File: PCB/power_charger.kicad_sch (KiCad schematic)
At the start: 10 parts

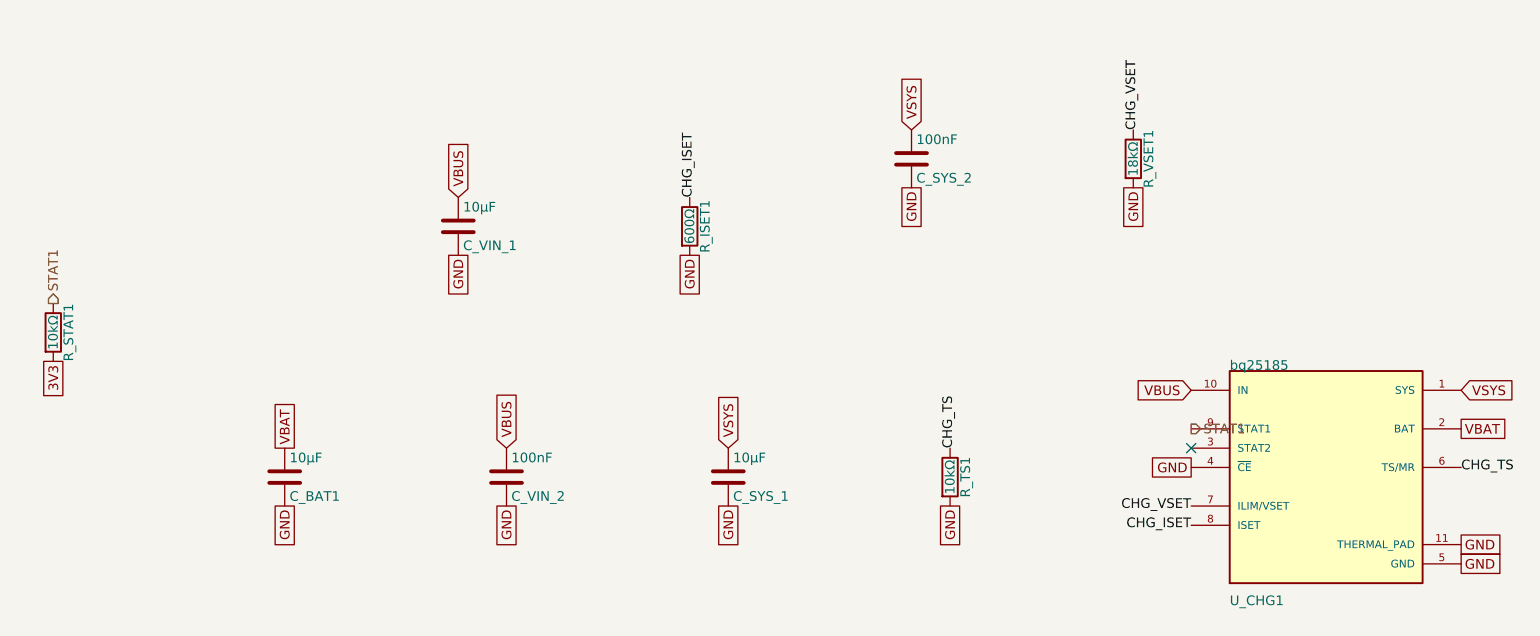
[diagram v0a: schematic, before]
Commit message: Fix footprints and begin layout (#17)
* refactor: updated gulikit footprint

This updates the gulikit thumbstick footprint to be accurate.

* layout: beginning pcb layout

This updates the schematic with a few different footprints while also starts the layout.
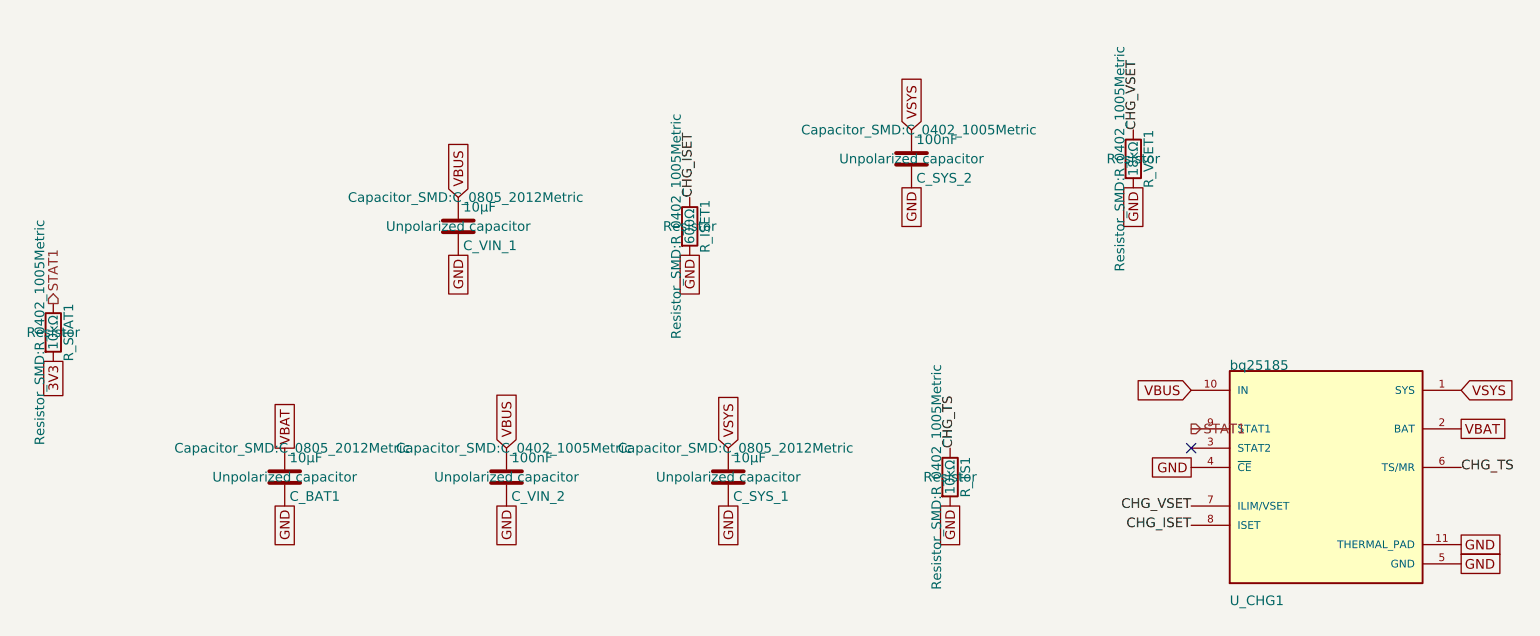
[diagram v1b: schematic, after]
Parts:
- U_CHG1: Description_1 1-cell, 1-A stand-alone linear battery charger with power p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 -> (none)

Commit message: refactor: swap footprints and add symmetry
This updates the footprints of a couple components to be smaller and closer to what we want. It also adds two buttons to ensure left and right side symmetry.
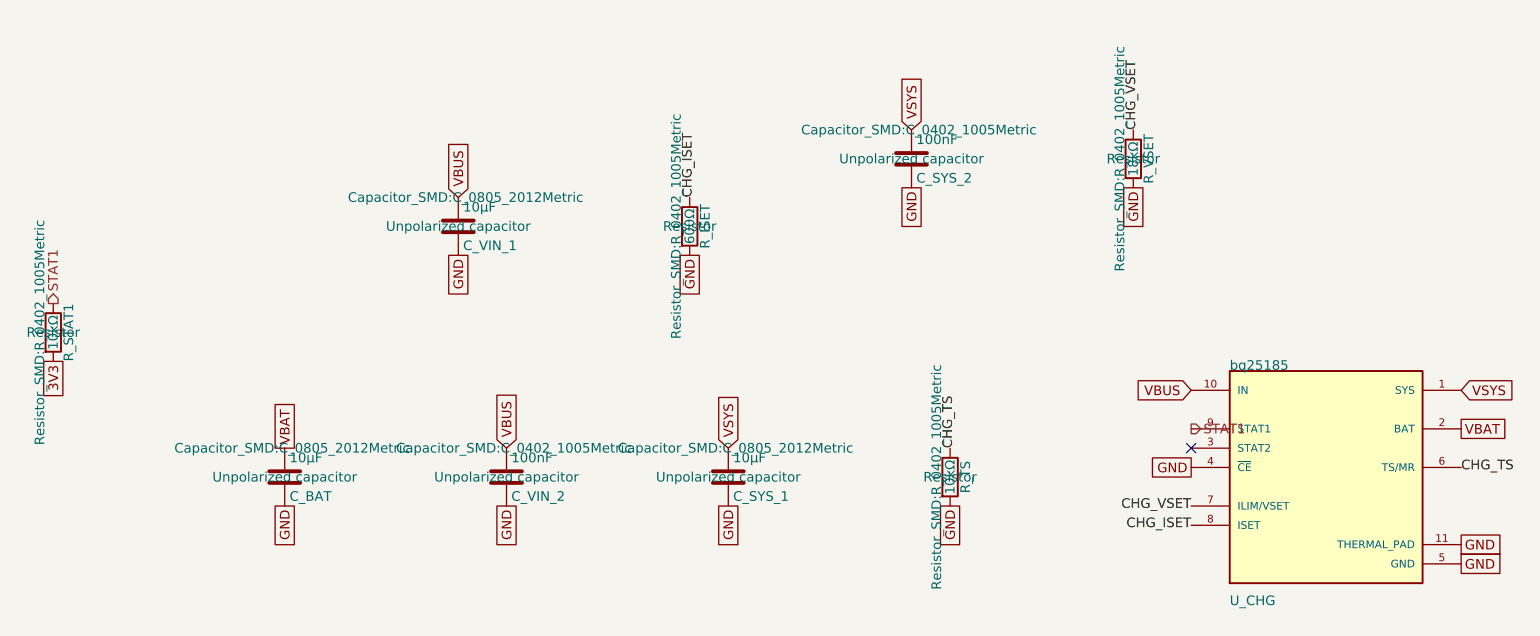
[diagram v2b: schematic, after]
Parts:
- removed C_BAT1: 10µF, Capacitor_SMD:C_0805_2012Metric, symbol Device:C
- removed R_ISET1: 600Ω, Resistor_SMD:R_0402_1005Metric, symbol Device:R
- removed R_TS1: 10kΩ, Resistor_SMD:R_0402_1005Metric, symbol Device:R
- removed R_VSET1: 18kΩ, Resistor_SMD:R_0402_1005Metric, symbol Device:R
- removed U_CHG1: bq25185, BQ25185DLHR:IC_BQ25185DLHR, symbol BQ25185DLHR:BQ25185DLHR
- added C_BAT: 10µF, Capacitor_SMD:C_0805_2012Metric, symbol Device:C
- added R_ISET: 600Ω, Resistor_SMD:R_0402_1005Metric, symbol Device:R
- added R_TS: 10kΩ, Resistor_SMD:R_0402_1005Metric, symbol Device:R
- added R_VSET: 18kΩ, Resistor_SMD:R_0402_1005Metric, symbol Device:R
- added U_CHG: bq25185, BQ25185DLHR:IC_BQ25185DLHR, symbol BQ25185DLHR:BQ25185DLHR
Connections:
- net CHG_ISET: now also R_ISET.1, U_CHG.8 (ISET)
- net CHG_TS: now also R_TS.1, U_CHG.6 (TS/MR)
- net CHG_VSET: now also R_VSET.1, U_CHG.7 (ILIM/VSET)
- net GND: now also C_BAT.2, R_ISET.2, R_TS.2, R_VSET.2, U_CHG.11 (THERMAL_PAD), U_CHG.4 (~{CE}), U_CHG.5 (GND)
- net STAT1: now also U_CHG.9 (STAT1)
- net VBAT: now also C_BAT.1, U_CHG.2 (BAT)
- net VBUS: now also U_CHG.10 (IN)
- net VSYS: now also U_CHG.1 (SYS)

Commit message: layout: everything is on the board
The board edge cuts are down to 100mm x 35mm. All the components have the right footprints and are on the board, but no traces exist yet, and not all circuits are laid out properly yet. Lots of DRC warnings.
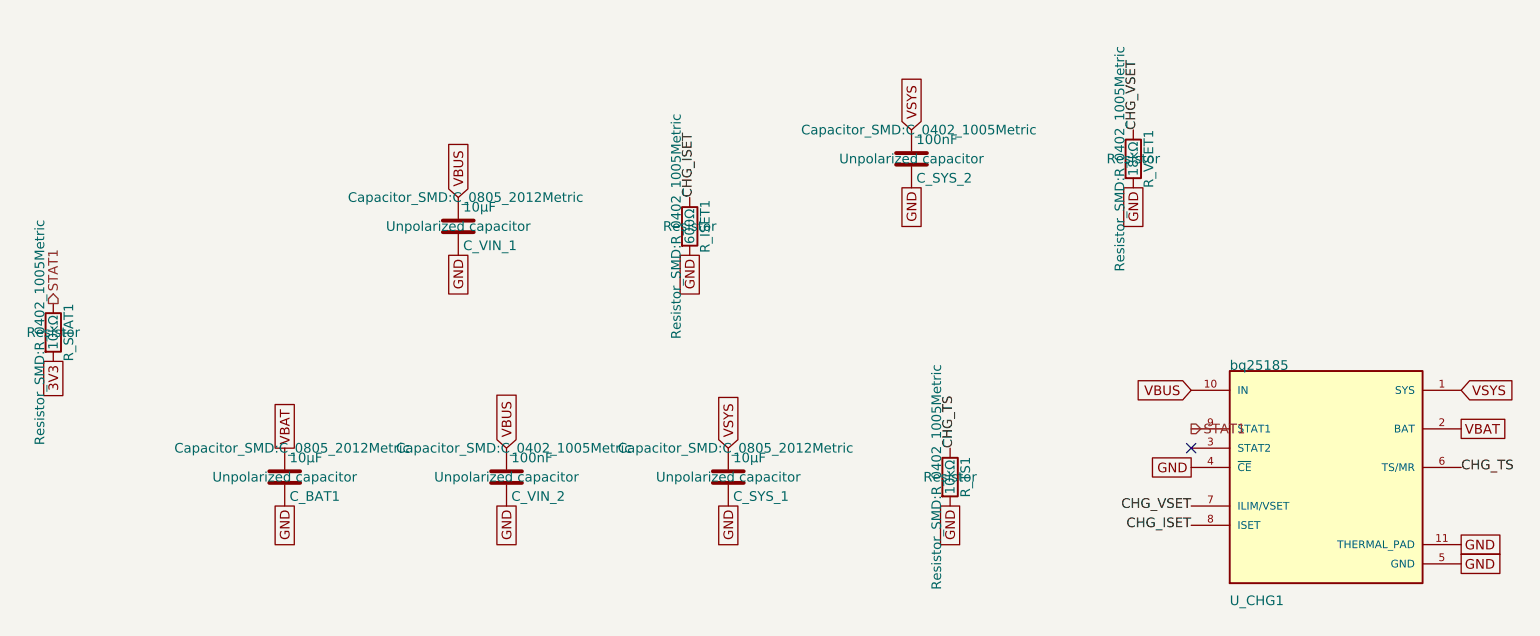
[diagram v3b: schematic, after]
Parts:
- removed C_BAT: 10µF, Capacitor_SMD:C_0805_2012Metric, symbol Device:C
- removed R_ISET: 600Ω, Resistor_SMD:R_0402_1005Metric, symbol Device:R
- removed R_TS: 10kΩ, Resistor_SMD:R_0402_1005Metric, symbol Device:R
- removed R_VSET: 18kΩ, Resistor_SMD:R_0402_1005Metric, symbol Device:R
- removed U_CHG: bq25185, BQ25185DLHR:IC_BQ25185DLHR, symbol BQ25185DLHR:BQ25185DLHR
- added C_BAT1: 10µF, Capacitor_SMD:C_0805_2012Metric, symbol Device:C
- added R_ISET1: 600Ω, Resistor_SMD:R_0402_1005Metric, symbol Device:R
- added R_TS1: 10kΩ, Resistor_SMD:R_0402_1005Metric, symbol Device:R
- added R_VSET1: 18kΩ, Resistor_SMD:R_0402_1005Metric, symbol Device:R
- added U_CHG1: bq25185, BQ25185DLHR:IC_BQ25185DLHR, symbol BQ25185DLHR:BQ25185DLHR
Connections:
- net CHG_ISET: now also R_ISET1.1, U_CHG1.8 (ISET)
- net CHG_TS: now also R_TS1.1, U_CHG1.6 (TS/MR)
- net CHG_VSET: now also R_VSET1.1, U_CHG1.7 (ILIM/VSET)
- net GND: now also C_BAT1.2, R_ISET1.2, R_TS1.2, R_VSET1.2, U_CHG1.11 (THERMAL_PAD), U_CHG1.4 (~{CE}), U_CHG1.5 (GND)
- net STAT1: now also U_CHG1.9 (STAT1)
- net VBAT: now also C_BAT1.1, U_CHG1.2 (BAT)
- net VBUS: now also U_CHG1.10 (IN)
- net VSYS: now also U_CHG1.1 (SYS)

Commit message: task: part number populated (#26)
kicad-happy run part 2 - MPN numbers populated
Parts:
- C_BAT1, C_SYS_1, C_VIN_1: MF (none) -> Yageo; Manufacturer_Part_Number (none) -> CC0805KRX5R7BB106
- C_SYS_2, C_VIN_2: MF (none) -> Yageo; Manufacturer_Part_Number (none) -> CC0402KRX7R9BB104
- R_ISET1: MF (none) -> Yageo; Manufacturer_Part_Number (none) -> RC0402FR-07600RL
- R_STAT1, R_TS1: MF (none) -> Yageo; Manufacturer_Part_Number (none) -> RC0402FR-0710KL
- R_VSET1: MF (none) -> Yageo; Manufacturer_Part_Number (none) -> RC0402FR-0718KL
- U_CHG1: Manufacturer_Part_Number (none) -> BQ25185DLHR
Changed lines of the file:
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@@
+			)
+		)
+		(property "MF" "Yageo" (at 0 0 0)
+			(effects
+				(font
+					(size 1.27 1.27)
+				)
+				(hide yes)
+			)
+		)
+		(property "Manufacturer_Part_Number" "RC0402FR-0718KL" (at 0 0 0)
+			(effects
+				(font
+					(size 1.27 1.27)
+				)
+				(hide yes)
 			)
 		)
@@
 			)
 		)
+		(property "MF" "Yageo" (at 0 0 0)
+			(effects
+				(font
+					(size 1.27 1.27)
+				)
+				(hide yes)
+			)
+		)
+		(property "Manufacturer_Part_Number" "CC0402KRX7R9BB104" (at 0 0 0)
+			(effects
+				(font
+					(size 1.27 1.27)
+				)
+				(hide yes)
+			)
+		)
 		(pin "1"
 		)
@@
 			)
 		)
+		(property "MF" "Yageo" (at 0 0 0)
+			(effects
+				(font
+					(size 1.27 1.27)
+				)
+				(hide yes)
+			)
+		)
+		(property "Manufacturer_Part_Number" "RC0402FR-0710KL" (at 0 0 0)
+			(effects
+				(font
+					(size 1.27 1.27)
+				)
+				(hide yes)
+			)
+		)
 		(pin "1"
 		)
@@
 			)
 		)
+		(property "MF" "Yageo" (at 0 0 0)
+			(effects
+				(font
+					(size 1.27 1.27)
+				)
+				(hide yes)
+			)
+		)
+		(property "Manufacturer_Part_Number" "CC0805KRX5R7BB106" (at 0 0 0)
+			(effects
+				(font
+					(size 1.27 1.27)
+				)
+				(hide yes)
+			)
+		)
 		(pin "1"
 		)
@@
 			)
 		)
+		(property "Manufacturer_Part_Number" "BQ25185DLHR" (at 0 0 0)
+			(effects
+				(font
+					(size 1.27 1.27)
+				)
+				(hide yes)
+			)
+		)
 		(pin "1"
 		)
@@
 			)
 		)
+		(property "MF" "Yageo" (at 0 0 0)
+			(effects
+				(font
+					(size 1.27 1.27)
+				)
+				(hide yes)
+			)
+		)
+		(property "Manufacturer_Part_Number" "CC0805KRX5R7BB106" (at 0 0 0)
+			(effects
+				(font
+					(size 1.27 1.27)
+				)
+				(hide yes)
+			)
+		)
 		(pin "1"
 		)
@@
 			)
 		)
+		(property "MF" "Yageo" (at 0 0 0)
+			(effects
+				(font
+					(size 1.27 1.27)
+				)
+				(hide yes)
+			)
+		)
+		(property "Manufacturer_Part_Number" "CC0402KRX7R9BB104" (at 0 0 0)
+			(effects
+				(font
+					(size 1.27 1.27)
+				)
+				(hide yes)
+			)
+		)
 		(pin "1"
 		)
@@
 			)
 		)
+		(property "MF" "Yageo" (at 0 0 0)
+			(effects
+				(font
+					(size 1.27 1.27)
+				)
+				(hide yes)
+			)
+		)
+		(property "Manufacturer_Part_Number" "RC0402FR-07600RL" (at 0 0 0)
+			(effects
+				(font
+					(size 1.27 1.27)
+				)
+				(hide yes)
+			)
+		)
 		(pin "1"
 		)
@@
 			)
 		)
+		(property "MF" "Yageo" (at 0 0 0)
+			(effects
+				(font
+					(size 1.27 1.27)
+				)
+				(hide yes)
+			)
+		)
+		(property "Manufacturer_Part_Number" "CC0805KRX5R7BB106" (at 0 0 0)
+			(effects
+				(font
+					(size 1.27 1.27)
+				)
+				(hide yes)
+			)
+		)
 		(pin "1"
 		)
@@
 			)
 		)
+		(property "MF" "Yageo" (at 0 0 0)
+			(effects
+				(font
+					(size 1.27 1.27)
+				)
+				(hide yes)
+			)
+		)
+		(property "Manufacturer_Part_Number" "RC0402FR-0710KL" (at 0 0 0)
+			(effects
+				(font
+					(size 1.27 1.27)
+				)
+				(hide yes)
+			)
+		)

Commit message: refactor: added STAT2
It was worth adding and will give us more info during battery charging.
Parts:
- added R_STAT2: 10kΩ, Resistor_SMD:R_0402_1005Metric, symbol Device:R
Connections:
- net 3V3: now also R_STAT2.2
- net STAT2: now reaches U_CHG1.3 (STAT2)
- net STAT2: now also R_STAT2.1
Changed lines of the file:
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@@
+		)
+	)
+	(hierarchical_label "STAT2"
+		(shape output)
+		(at 214.63 121.92 0)
+		(effects
+			(font
+				(size 1.27 1.27)
+			)
+			(justify left)
 		)
 	)
@@
 					(unit 1)
 				)
+			)
+		)
+	)
+	(hierarchical_label "STAT2"
+		(shape output)
+		(at 80.01 102.87 90)
+		(effects
+			(font
+				(size 1.27 1.27)
+			)
+			(justify left)
+		)
+	)
+	(global_label "3V3"
+		(shape passive)
+		(at 80.01 110.49 270)
+		(fields_autoplaced yes)
+		(effects
+			(font
+				(size 1.27 1.27)
+			)
+			(justify right)
+		)
+	)
+	(symbol
+		(lib_id "Device:R")
+		(at 80.01 106.68 0)
+		(unit 1)
+		(body_style 1)
+		(exclude_from_sim no)
+		(in_bom yes)
+		(on_board yes)
+		(in_pos_files yes)
+		(dnp no)
+		(fields_autoplaced yes)
+		(property "Reference" "R_STAT2"
+			(at 82.042 106.68 90)
+			(show_name no)
+			(do_not_autoplace no)
+			(effects
+				(font
+					(size 1.27 1.27)
+				)
+			)
+		)
+		(property "Value" "10kΩ"
+			(at 80.01 106.68 90)
+			(show_name no)
+			(do_not_autoplace no)
+			(effects
+				(font
+					(size 1.27 1.27)
+				)
+			)
+		)
+		(property "Footprint" "Resistor_SMD:R_0402_1005Metric"
+			(at 78.232 106.68 90)
+			(show_name no)
+			(do_not_autoplace no)
+			(effects
+				(font
+					(size 1.27 1.27)
+				)
+			)
+		)
+		(property "Datasheet" ""
+			(at 80.01 106.68 0)
+			(show_name no)
+			(do_not_autoplace no)
+			(effects
+				(font
+					(size 1.27 1.27)
+				)
+			)
+		)
+		(property "Description" "Resistor"
+			(at 80.01 106.68 0)
+			(show_name no)
+			(do_not_autoplace no)
+			(effects
+				(font
+					(size 1.27 1.27)
+				)
+			)
+		)
+		(property "MF" "Yageo"
+			(at 0 0 0)
+			(hide yes)
+			(show_name no)
+			(do_not_autoplace no)
+			(effects
+				(font
+					(size 1.27 1.27)
+				)
+			)
+		)
+		(property "Manufacturer_Part_Number" "RC0402FR-0710KL"
+			(at 0 0 0)
+			(hide yes)
+			(show_name no)
+			(do_not_autoplace no)
+			(effects
+				(font
+					(size 1.27 1.27)
+				)
+			)
+		)
+		(pin "1"
+		)
+		(pin "2"
+		)
+		(instances
+			(project "snips_controller"
+				(path "/21935953-32a0-46ad-8079-8177920c6978/a161eba2-5cf9-4e54-b23a-cab3e9f70ed0"
+					(reference "R_STAT2")
+					(unit 1)
+				)
